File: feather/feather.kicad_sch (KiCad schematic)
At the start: 135 parts, among them CN1 ST-0337D00-071-1A2H, CN2 GT-3321667P-01, J1 Connector, USB-TYPE-C-16P, SW1 1TS015A-1400-0600-CT, SW2 1TS015A-1400-0600-CT, U1 TLV76733DRVx, U10 OPA1622, U11 OPA1622, U2 LM27762, U3 TAD5242IRGER, U4 TLV76733DRVx, U5 OPA1612AxD, U6 RP2350A-QFN60, U7 OPA1612AxD, U8 OPA1612AxD, U9 OPA1622, X1 12MHz

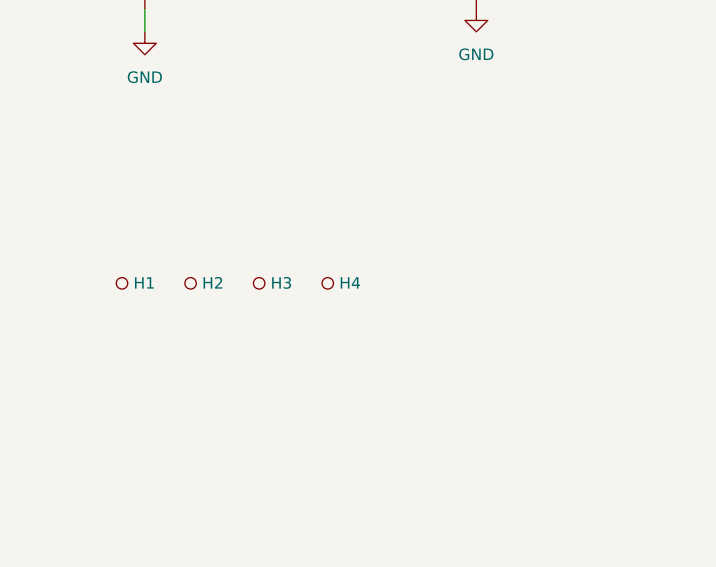
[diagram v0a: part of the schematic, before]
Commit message: feat: update pcb design and layout
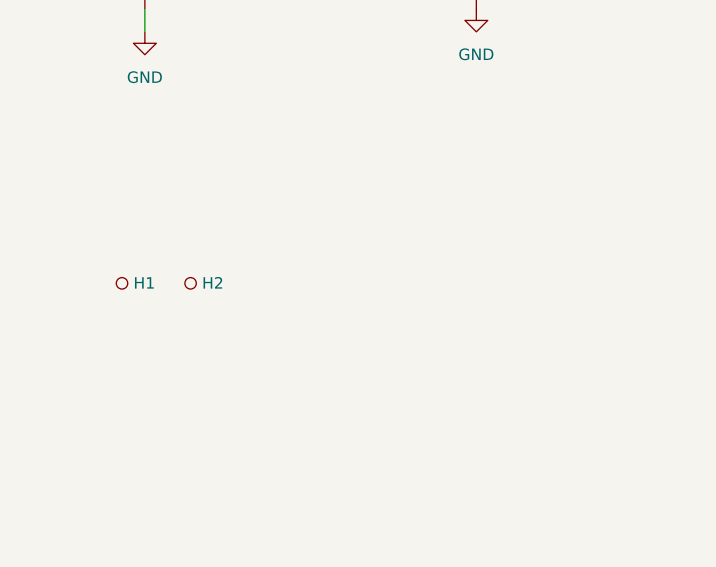
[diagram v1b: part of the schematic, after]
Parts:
- removed H3, H4: (no value), PCM_JLCPCB:Hole_Tooling_JLCPCB, symbol PCM_JLCPCB-Manufacturing:Tooling Hole, PCM_JLCPCB, 1.152mm
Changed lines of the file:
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@@
 	)
 	(symbol
-		(lib_id "PCM_JLCPCB-Manufacturing:Tooling Hole, PCM_JLCPCB, 1.152mm")
-		(at 55.88 320.04 0)
-		(unit 1)
-		(body_style 1)
-		(exclude_from_sim no)
-		(in_bom yes)
-		(on_board yes)
-		(in_pos_files yes)
-		(dnp no)
-		(fields_autoplaced yes)
-		(property "Reference" "H4"
-			(at 57.15 320.0399 0)
-			(show_name no)
-			(do_not_autoplace no)
-			(effects
-				(font
-					(size 1.27 1.27)
-				)
-				(justify left)
-			)
-		)
-		(property "Value" ""
-			(at 55.88 320.04 0)
-			(show_name no)
-			(do_not_autoplace no)
-			(effects
-				(font
-					(size 1.27 1.27)
-				)
-			)
-		)
-		(property "Footprint" "PCM_JLCPCB:Hole_Tooling_JLCPCB"
-			(at 55.88 320.04 0)
-			(hide yes)
-			(show_name no)
-			(do_not_autoplace no)
-			(effects
-				(font
-					(size 1.27 1.27)
-				)
-			)
-		)
-		(property "Datasheet" "https://jlcpcb.com/help/article/How-to-add-tooling-holes-for-PCB-assembly-order"
-			(at 55.88 320.04 0)
-			(hide yes)
-			(show_name no)
-			(do_not_autoplace no)
-			(effects
-				(font
-					(size 1.27 1.27)
-				)
-			)
-		)
-		(property "Description" "1. Two or three tooling holes should be added on the PCB, they should be placed in opposite corners of the PCB and as far apart from one another as practical. 2. Tooling holes should be 1.152mm(45.4mil) round non-plated holes with 0.148mm solder mask expansion. 3. Tooling holes are only required for PCB assembly orders. 4. Please try to add tooling holes on empty space and keep them away from traces. If there is no enough room, you can add them to the copper area."
-			(at 55.88 320.04 0)
-			(hide yes)
-			(show_name no)
-			(do_not_autoplace no)
-			(effects
-				(font
-					(size 1.27 1.27)
-				)
-			)
-		)
-		(instances
-			(project "feather"
-				(path "/de39cee1-e9de-4f04-8d7c-52ac20337d6d"
-					(reference "H4")
-					(unit 1)
-				)
-			)
-		)
-	)
-	(symbol
 		(lib_id "PCM_JLCPCB-Capacitors:0402,100nF")
 		(at 109.22 110.49 0)
@@
 					(unit 1)
 				)
-			)
-		)
-	)
-	(symbol
-		(lib_id "PCM_JLCPCB-Manufacturing:Tooling Hole, PCM_JLCPCB, 1.152mm")
-		(at 48.26 320.04 0)
-		(unit 1)
-		(body_style 1)
-		(exclude_from_sim no)
-		(in_bom yes)
-		(on_board yes)
-		(in_pos_files yes)
-		(dnp no)
-		(fields_autoplaced yes)
-		(property "Reference" "H3"
-			(at 49.53 320.0399 0)
-			(show_name no)
-			(do_not_autoplace no)
-			(effects
-				(font
-					(size 1.27 1.27)
-				)
-				(justify left)
-			)
-		)
-		(property "Value" ""
-			(at 48.26 320.04 0)
-			(show_name no)
-			(do_not_autoplace no)
-			(effects
-				(font
-					(size 1.27 1.27)
-				)
-			)
-		)
-		(property "Footprint" "PCM_JLCPCB:Hole_Tooling_JLCPCB"
-			(at 48.26 320.04 0)
-			(hide yes)
-			(show_name no)
-			(do_not_autoplace no)
-			(effects
-				(font
-					(size 1.27 1.27)
-				)
-			)
-		)
-		(property "Datasheet" "https://jlcpcb.com/help/article/How-to-add-tooling-holes-for-PCB-assembly-order"
-			(at 48.26 320.04 0)
-			(hide yes)
-			(show_name no)
-			(do_not_autoplace no)
-			(effects
-				(font
-					(size 1.27 1.27)
-				)
-			)
-		)
-		(property "Description" "1. Two or three tooling holes should be added on the PCB, they should be placed in opposite corners of the PCB and as far apart from one another as practical. 2. Tooling holes should be 1.152mm(45.4mil) round non-plated holes with 0.148mm solder mask expansion. 3. Tooling holes are only required for PCB assembly orders. 4. Please try to add tooling holes on empty space and keep them away from traces. If there is no enough room, you can add them to the copper area."
-			(at 48.26 320.04 0)
-			(hide yes)
-			(show_name no)
-			(do_not_autoplace no)
-			(effects
-				(font
-					(size 1.27 1.27)
-				)
-			)
-		)
-		(instances
-			(project "feather"
-				(path "/de39cee1-e9de-4f04-8d7c-52ac20337d6d"
-					(reference "H3")
-					(unit 1)
-				)

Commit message: feat: update feather design files
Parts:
- C32: LCSC C307331 -> C1525
- CN1: LCSC (none) -> C2829972
- CN2: LCSC (none) -> C2762984
- D1: LCSC (none) -> C89411
- D10, D11, D6, D7, D8, D9: LCSC (none) -> C48260
- F1: LCSC (none) -> C207016
- L1: LCSC (none) -> C42411119
- SW1, SW2: LCSC (none) -> C319433
- U1, U4: LCSC (none) -> C2848334
- U10, U11, U9: LCSC (none) -> C2876559
- U2: LCSC (none) -> C473398
- U3: LCSC (none) -> C42414591
- U5, U7, U8: LCSC (none) -> C2058640
- U6: LCSC (none) -> C42411118

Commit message: feat: add two more buttons
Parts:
- added D6, D9: TPD1E10B06DPYR, TPD1E10B06DPYR:DIO_TPD1E10B06DPYR, symbol TPD1E10B06DPYR:TPD1E10B06DPYR
- added R38, R39: 1kΩ, PCM_JLCPCB:R_0402, symbol PCM_JLCPCB-Resistors:0402,1kΩ
- added SW3, SW4: 1TS015A-1400-0600-CT, easyeda2kicad:SW-SMD_L3.0-W2.0-LS3.5, symbol easyeda2kicad:1TS015A-1400-0600-CT
- H1, H2: now left out of the parts list
- R32: value 10kΩ -> 1kΩ; symbol PCM_JLCPCB-Resistors:0402,10kΩ -> PCM_JLCPCB-Resistors:0402,1kΩ; LCSC C25744 -> C11702; Part 0402WGF1002TCE -> 0402WGF1001TCE; Resistance 10kΩ -> 1kΩ; Stock 24372091 -> 13226393
- R33: value 4.7kΩ -> 100kΩ; symbol PCM_JLCPCB-Resistors:0402,4.7kΩ -> PCM_JLCPCB-Resistors:0402,100kΩ; LCSC C25900 -> C25741; Part 0402WGF4701TCE -> 0402WGF1003TCE; Resistance 4.7kΩ -> 100kΩ; Stock 7644059 -> 6969783
- R41: value 470Ω -> 330Ω; symbol PCM_JLCPCB-Resistors:0402,470Ω -> PCM_JLCPCB-Resistors:0402,330Ω; LCSC C25117 -> C25104; Part 0402WGF4700TCE -> 0402WGF3300TCE; Resistance 470Ω -> 330Ω; Stock 1007760 -> 1159127
- R46: renamed from R44; value 10kΩ -> 1kΩ; symbol PCM_JLCPCB-Resistors:0402,10kΩ -> PCM_JLCPCB-Resistors:0402,1kΩ; LCSC C25744 -> C11702; Part 0402WGF1002TCE -> 0402WGF1001TCE; Resistance 10kΩ -> 1kΩ; Stock 24372091 -> 13226393
- R51: renamed from R49; value 4.7kΩ -> 100kΩ; symbol PCM_JLCPCB-Resistors:0402,4.7kΩ -> PCM_JLCPCB-Resistors:0402,100kΩ; LCSC C25900 -> C25741; Part 0402WGF4701TCE -> 0402WGF1003TCE; Resistance 4.7kΩ -> 100kΩ; Stock 7644059 -> 6969783
- U6: value RP2350A-QFN60 -> RP2354A
- renumbered D8 to D10, D9 to D11, D10 to D12, D11 to D13, D6 to D7, D7 to D8, R38 to R44, R39 to R45, R45 to R47, R46 to R48, R47 to R49, R48 to R50, R50 to R52, R51 to R53, R52 to R54, R53 to R55
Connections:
- net GND: now also D6.2, D9.2, SW3.1, SW4.1
- net GP0: now also R38.1
- net GP1: now also R39.1
- net GP10: now also D6.1
- net GP11: now also D9.1
- new net: R39.2, SW4.2
- new net: R38.2, SW3.2
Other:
- note added: "3.5mm single-ended jack"
- note added: "4.4mm differential jack"
- note added: "5V to 3V3 LDO"
- note added: "5V to 3V3 LDO for DAC"
- note added: "DAC (Clock)"
- note added: "DAC (Data)"
- note added: "DAC (FSYNC / WS)"
- note added: "OPA1612 op-amp for differential (1)"
- note added: "OPA1612 op-amp for differential (2)"
- note added: "OPA1612 op-amp for single-ended"
- note added: "OPA1622 differential Enable control"
- note added: "OPA1622 headphone amp for differential (1)"
- note added: "OPA1622 headphone amp for differential (2)"
- note added: "OPA1622 headphone amp for single-ended"
- note added: "PCBA tooling holes"
- note added: "RP2354 control buttons"
- note added: "RP2354A MCU"
- note added: "Status light"
- note added: "TAD5242 DAC"
- note added: "USB C connector"
- note added: "USB ESD protection"
- note added: "Volume control buttons"
- note added: "Volume down button"
- note added: "Volume up button"
- note added: "±4.5V charge pump & LDO"
- note removed: "Balanced output 1 headphone amp"
- note removed: "Balanced output 1 op-amp"
- note removed: "Balanced output 2 headphone amp"
- note removed: "Balanced output 2 op-amp"
- note removed: "DAC"
- note removed: "Unbalanced output headphone amp"
- note removed: "Unbalanced output op-amp"
- company: (none) -> LightWolf
- title: (none) -> Feather USB DAC card
- moved on the sheet: C10, C13, C15, C16, C17, C19, C2, C20, C21, C22, C23, C24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
